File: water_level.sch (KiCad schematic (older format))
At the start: 13 parts, among them U4 TLP293-4

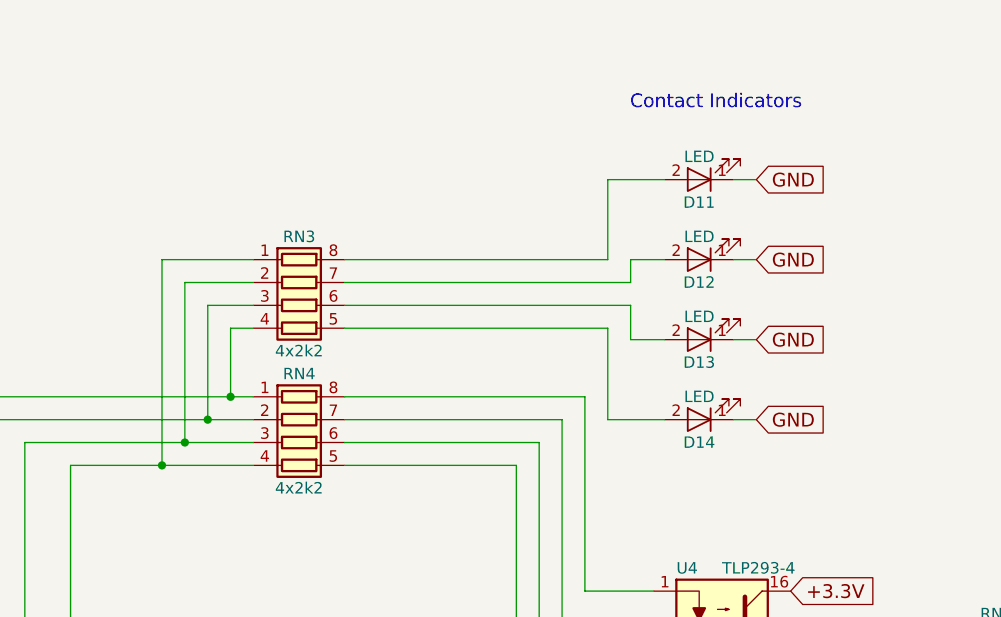
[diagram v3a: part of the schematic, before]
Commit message: the components roughly spaced on the pcb
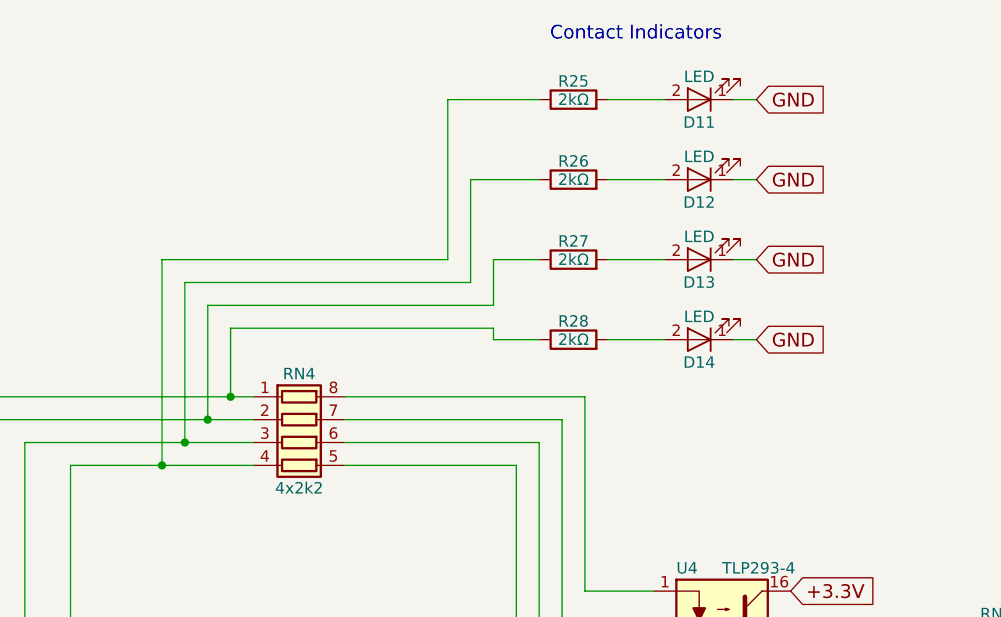
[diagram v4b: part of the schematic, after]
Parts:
- removed RN3: 4x2k2, kilibs:YC164-Yageo-Handsoldering, symbol R_Pack04
- added R25, R26, R27, R28: 2kΩ, Resistors_SMD:R_0603_HandSoldering, symbol R
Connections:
- net at RN4.2 (R2.1), SENS_2.4 (NC): now also R27.1
- net at RN4.1 (R1.1), SENS_1.4 (NC): now also R28.1
- net at RN4.3 (R3.1), SENS_3.4 (NC): now also R26.1
- net at RN4.4 (R4.1), SENS_4.4 (NC): now also R25.1
- net at D13.2 (A): now also R27.2
- net at D14.2 (A): now also R28.2
- net at D12.2 (A): now also R26.2
- net at D11.2 (A): now also R25.2
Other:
- moved on the sheet: D11, D12, D13, D14
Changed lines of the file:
@@
 L LED D13
 U 1 1 59403F87
+P 8000 2100
+F 0 "D13" H 8000 2200 50  0000 C CNN
+F 1 "LED" H 8000 2000 50  0000 C CNN
+F 2 "LEDs:LED_1206" H 8000 2100 50  0001 C CNN
+F 3 "http://hu.farnell.com/lumex/sml-lx15syc-tr/led-yellow-3mm-60mcd-590nm/dp/2062220" H 8000 2100 50  0001 C CNN
+	1    8000 2100
+	-1   0    0    1
+$EndComp
+Wire Wire Line
+	8250 2100 8150 2100
+$Comp
+L LED D14
+U 1 1 5940539F
 P 8000 2450
-F 0 "D13" H 8000 2550 50  0000 C CNN
+F 0 "D14" H 8000 2550 50  0000 C CNN
 F 1 "LED" H 8000 2350 50  0000 C CNN
 F 2 "LEDs:LED_1206" H 8000 2450 50  0001 C CNN
@@
 	8250 2450 8150 2450
 $Comp
-L LED D14
-U 1 1 5940539F
-P 8000 2800
-F 0 "D14" H 8000 2900 50  0000 C CNN
-F 1 "LED" H 8000 2700 50  0000 C CNN
-F 2 "LEDs:LED_1206" H 8000 2800 50  0001 C CNN
-F 3 "http://hu.farnell.com/lumex/sml-lx15syc-tr/led-yellow-3mm-60mcd-590nm/dp/2062220" H 8000 2800 50  0001 C CNN
-	1    8000 2800
-	-1   0    0    1
-$EndComp
-Wire Wire Line
-	8250 2800 8150 2800
-$Comp
 L LED D12
 U 1 1 59405535
-P 8000 2100
-F 0 "D12" H 8000 2200 50  0000 C CNN
-F 1 "LED" H 8000 2000 50  0000 C CNN
-F 2 "LEDs:LED_1206" H 8000 2100 50  0001 C CNN
-F 3 "http://hu.farnell.com/lumex/sml-lx15syc-tr/led-yellow-3mm-60mcd-590nm/dp/2062220" H 8000 2100 50  0001 C CNN
-	1    8000 2100
-	-1   0    0    1
-$EndComp
-Wire Wire Line
-	8250 2100 8150 2100
-$Comp
-L LED D11
-U 1 1 59405613
 P 8000 1750
-F 0 "D11" H 8000 1850 50  0000 C CNN
+F 0 "D12" H 8000 1850 50  0000 C CNN
 F 1 "LED" H 8000 1650 50  0000 C CNN
 F 2 "LEDs:LED_1206" H 8000 1750 50  0001 C CNN
@@
 Wire Wire Line
 	8250 1750 8150 1750
-Text Notes 8450 1450 2    60   ~ 0
+$Comp
+L LED D11
+U 1 1 59405613
+P 8000 1400
+F 0 "D11" H 8000 1500 50  0000 C CNN
+F 1 "LED" H 8000 1300 50  0000 C CNN
+F 2 "LEDs:LED_1206" H 8000 1400 50  0001 C CNN
+F 3 "http://hu.farnell.com/lumex/sml-lx15syc-tr/led-yellow-3mm-60mcd-590nm/dp/2062220" H 8000 1400 50  0001 C CNN
+	1    8000 1400
+	-1   0    0    1
+$EndComp
+Wire Wire Line
+	8250 1400 8150 1400
+Text Notes 8100 1150 2    60   ~ 0
 Contact Indicators
+Text GLabel 8250 1400 2    60   Input ~ 0
+GND
 Text GLabel 8250 1750 2    60   Input ~ 0
 GND
@@
 GND
 Text GLabel 8250 2450 2    60   Input ~ 0
-GND
-Text GLabel 8250 2800 2    60   Input ~ 0
 GND
 Text GLabel 3100 4100 0    60   Input ~ 0
@@
 $EndComp
 Wire Wire Line
-	6450 2100 7600 2100
-Wire Wire Line
-	7600 2100 7600 1750
-Wire Wire Line
-	7600 1750 7850 1750
-Wire Wire Line
-	6450 2200 7700 2200
-Wire Wire Line
-	7700 2200 7700 2100
-Wire Wire Line
-	7700 2100 7850 2100
-Wire Wire Line
-	6450 2300 7700 2300
-Wire Wire Line
-	7700 2300 7700 2450
-Wire Wire Line
-	7700 2450 7850 2450
-Wire Wire Line
-	6450 2400 7600 2400
-Wire Wire Line
-	7600 2400 7600 2800
-Wire Wire Line
-	7600 2800 7850 2800
+	7600 1400 7850 1400
+Wire Wire Line
+	7600 2450 7850 2450
 Wire Wire Line
 	4650 3300 4650 2700
@@
 Connection ~ 5650 3000
 Wire Wire Line
-	5950 2400 6050 2400
-Wire Wire Line
-	5850 2300 6050 2300
-Wire Wire Line
-	5750 2200 6050 2200
-Wire Wire Line
-	5650 2100 6050 2100
-$Comp
-L R_Pack04 RN3
-U 1 1 59A818FC
-P 6250 2300
-F 0 "RN3" V 5950 2300 50  0000 C CNN
-F 1 "4x2k2" V 6450 2300 50  0000 C CNN
-F 2 "kilibs:YC164-Yageo-Handsoldering" V 6525 2300 50  0001 C CNN
-F 3 "http://hu.farnell.com/yageo-phycomp/yc164-jr-072k2l/resistor-array-arv241-1206-2k2/dp/9234535" H 6250 2300 50  0001 C CNN
-	1    6250 2300
-	0    1    1    0
-$EndComp
+	5950 2400 7100 2400
+Wire Wire Line
+	5850 2300 7100 2300
+Wire Wire Line
+	5750 2200 7000 2200
+Wire Wire Line
+	5650 2100 6900 2100
 $Comp
 L R_Pack04 RN4
@@
 Wire Wire Line
 	9050 4050 9050 4650
+$Comp
+L R R25
+U 1 1 59AB9E05
+P 7450 1400
+F 0 "R25" V 7530 1400 50  0000 C CNN
+F 1 "2kΩ" V 7450 1400 50  0000 C CNN
+F 2 "Resistors_SMD:R_0603_HandSoldering" V 7380 1400 50  0001 C CNN
+F 3 "hu.farnell.com/multicomp/mcwr06x2001ftl/res-thick-film-2k-1-0-1w-0603/dp/2447319" H 7450 1400 50  0001 C CNN
+	1    7450 1400
+	0    -1   -1   0
+$EndComp
+$Comp
+L R R26
+U 1 1 59ABA119
+P 7450 1750
+F 0 "R26" V 7530 1750 50  0000 C CNN
+F 1 "2kΩ" V 7450 1750 50  0000 C CNN
+F 2 "Resistors_SMD:R_0603_HandSoldering" V 7380 1750 50  0001 C CNN
+F 3 "hu.farnell.com/multicomp/mcwr06x2001ftl/res-thick-film-2k-1-0-1w-0603/dp/2447319" H 7450 1750 50  0001 C CNN
+	1    7450 1750
+	0    -1   -1   0
+$EndComp
+$Comp
+L R R27
+U 1 1 59ABA15D
+P 7450 2100
+F 0 "R27" V 7530 2100 50  0000 C CNN
+F 1 "2kΩ" V 7450 2100 50  0000 C CNN
+F 2 "Resistors_SMD:R_0603_HandSoldering" V 7380 2100 50  0001 C CNN
+F 3 "hu.farnell.com/multicomp/mcwr06x2001ftl/res-thick-film-2k-1-0-1w-0603/dp/2447319" H 7450 2100 50  0001 C CNN
+	1    7450 2100
+	0    -1   -1   0
+$EndComp
+$Comp
+L R R28
+U 1 1 59ABA30D
+P 7450 2450
+F 0 "R28" V 7530 2450 50  0000 C CNN
+F 1 "2kΩ" V 7450 2450 50  0000 C CNN
+F 2 "Resistors_SMD:R_0603_HandSoldering" V 7380 2450 50  0001 C CNN
+F 3 "hu.farnell.com/multicomp/mcwr06x2001ftl/res-thick-film-2k-1-0-1w-0603/dp/2447319" H 7450 2450 50  0001 C CNN
+	1    7450 2450
+	0    -1   -1   0
+$EndComp
+Wire Wire Line
+	7600 1750 7850 1750
+Wire Wire Line
+	7600 2100 7850 2100
+Wire Wire Line
+	7300 2450 7100 2450
+Wire Wire Line
+	7100 2450 7100 2400
+Wire Wire Line
+	7300 2100 7100 2100
+Wire Wire Line
+	7100 2100 7100 2300
+Wire Wire Line
+	7300 1750 7000 1750
+Wire Wire Line
+	7000 1750 7000 2200
+Wire Wire Line
+	7300 1400 6900 1400
+Wire Wire Line
+	6900 1400 6900 2100
 $EndSCHEMATC

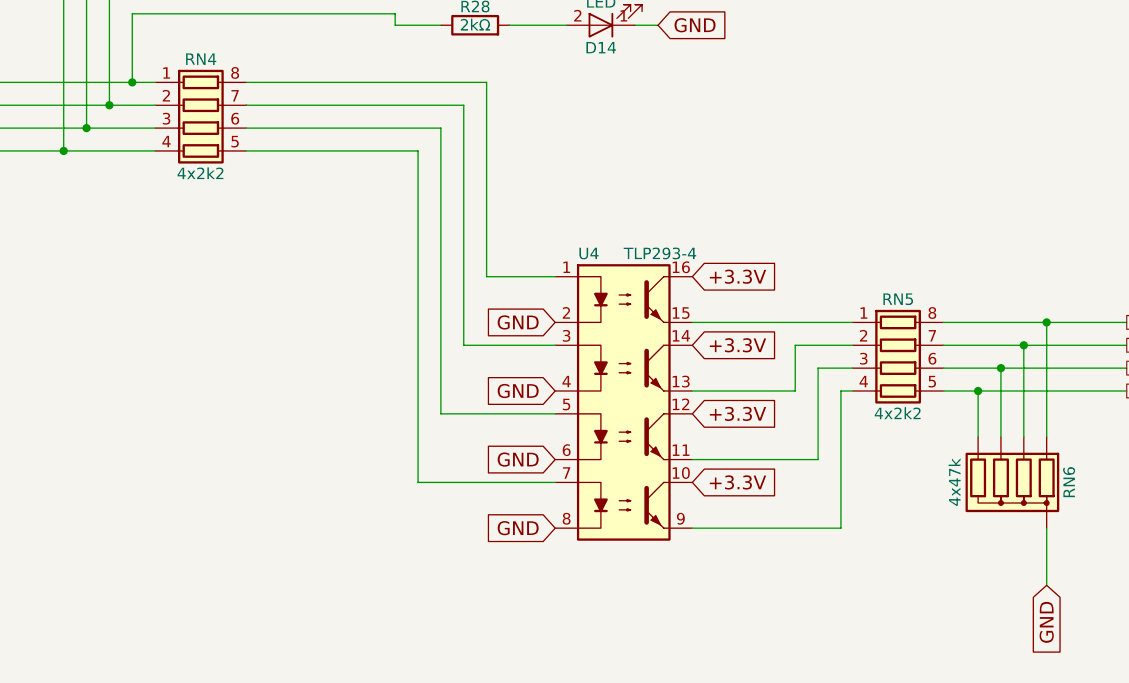
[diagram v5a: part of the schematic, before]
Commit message: This version contains the final revision before the part footprint verification.
- The fuse is now moved outside of the power module before any parts
- The wifi module has an additional pair of 22R differential resistors
- The minor moves in the power power supply of the wifi module
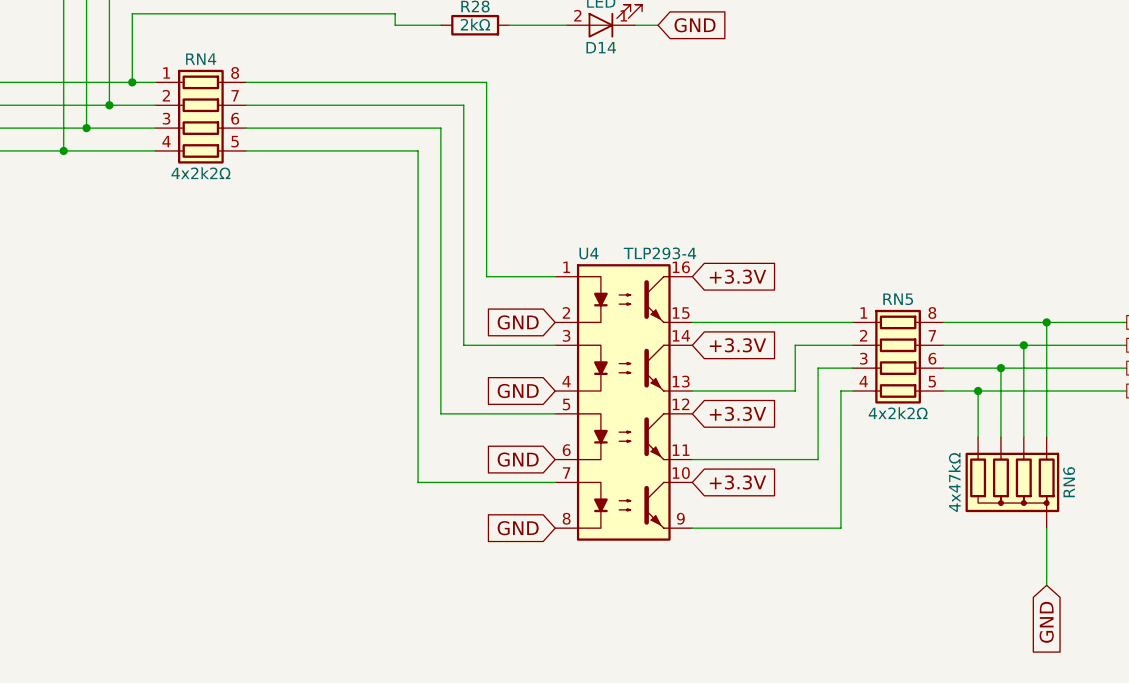
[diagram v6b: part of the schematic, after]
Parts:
- RN4, RN5: value 4x2k2 -> 4x2k2Ω
- RN6: value 4x47k -> 4x47kΩ
- U4: footprint Housings_SOIC:SOIC-16_3.9x9.9mm_Pitch1.27mm -> Housings_DIP:DIP-16_W7.62mm_SMDSocket_SmallPads; alt_soic (none) -> http://hu.farnell.com/toshiba/tlp293-4-gb/optocoupler-photo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
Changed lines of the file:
@@
 P 9750 4450
 F 0 "RN6" V 9450 4450 50  0000 C CNN
-F 1 "4x47k" V 9950 4450 50  0000 C CNN
+F 1 "4x47kΩ" V 9950 4450 50  0000 C CNN
 F 2 "water:YC158-Yageo-Handsoldering" V 10025 4450 50  0001 C CNN
 F 3 "http://hu.farnell.com/yageo-phycomp/yc158tjr-0747kl/resistor-network-rna310-1206-47k/dp/9236279" H 9750 4450 50  0001 C CNN
@@
 F 0 "U4" H 7900 4850 50  0000 L CNN
 F 1 "TLP293-4" H 8100 4850 50  0000 L CNN
-F 2 "Housings_SOIC:SOIC-16_3.9x9.9mm_Pitch1.27mm" H 7900 3550 50  0001 L CIN
-F 3 "http://hu.farnell.com/toshiba/tlp293-4-gb/optocoupler-phototrans-3-75kv/dp/2524320" H 8100 4050 50  0001 L CNN
+F 2 "Housings_DIP:DIP-16_W7.62mm_SMDSocket_SmallPads" H 7900 3550 50  0001 L CIN
+F 3 "http://hu.farnell.com/broadcom-limited/acpl-847-300e/optocoupler-transistor-o-p-5kv/dp/1339044" H 8100 4050 50  0001 L CNN
+F 4 "http://hu.farnell.com/toshiba/tlp293-4-gb/optocoupler-phototrans-3-75kv/dp/2524320" H 8100 4150 60  0001 C CNN "alt_soic"
 	1    8100 4150
 	1    0    0    -1
@@
 P 6250 2900
 F 0 "RN4" V 5950 2900 50  0000 C CNN
-F 1 "4x2k2" V 6450 2900 50  0000 C CNN
+F 1 "4x2k2Ω" V 6450 2900 50  0000 C CNN
 F 2 "kilibs:YC164-Yageo-Handsoldering" V 6525 2900 50  0001 C CNN
 F 3 "http://hu.farnell.com/yageo-phycomp/yc164-jr-072k2l/resistor-array-arv241-1206-2k2/dp/9234535" H 6250 2900 50  0001 C CNN
@@
 P 9300 3950
 F 0 "RN5" V 9000 3950 50  0000 C CNN
-F 1 "4x2k2" V 9500 3950 50  0000 C CNN
+F 1 "4x2k2Ω" V 9500 3950 50  0000 C CNN
 F 2 "kilibs:YC164-Yageo-Handsoldering" V 9575 3950 50  0001 C CNN
 F 3 "http://hu.farnell.com/yageo-phycomp/yc164-jr-072k2l/resistor-array-arv241-1206-2k2/dp/9234535" H 9300 3950 50  0001 C CNN

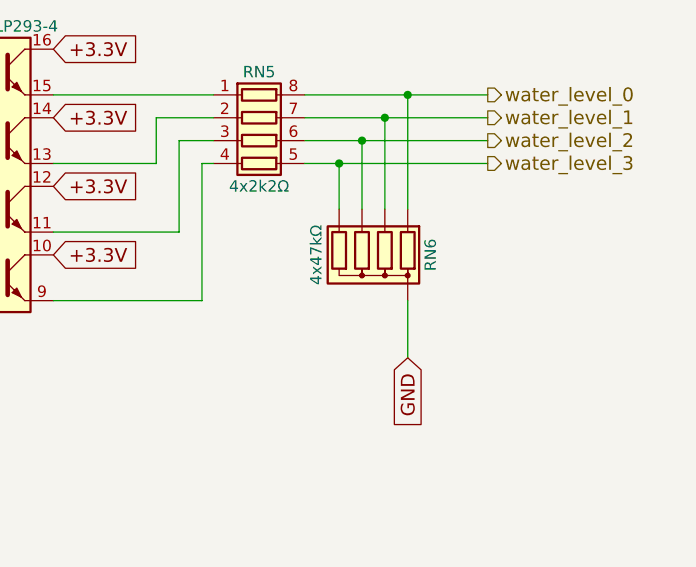
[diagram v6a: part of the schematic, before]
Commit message: I have replaced the 8xresistors to 4resistors because the distance between the pads was not big enough for the 3um copper layers
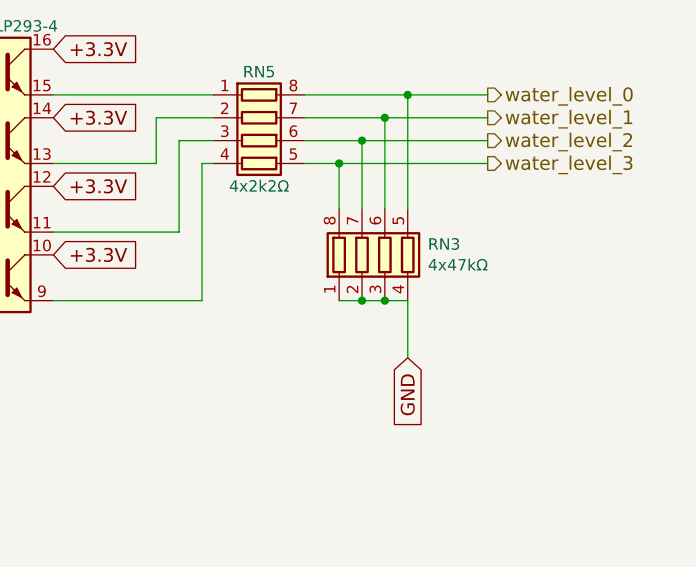
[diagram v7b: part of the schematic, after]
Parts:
- removed RN6: 4x47kΩ, water:YC158-Yageo-Handsoldering, symbol R_Network04
- added RN3: 4x47kΩ, kilibs:YC164-Yageo-Handsoldering, symbol R_Pack04
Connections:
- net GND: now also RN3.1 (R1.1), RN3.2 (R2.1), RN3.3 (R3.1), RN3.4 (R4.1)
- net water_level_0: now also RN3.5 (R4.2)
- net water_level_1: now also RN3.6 (R3.2)
- net water_level_2: now also RN3.7 (R2.2)
- net water_level_3: now also RN3.8 (R1.2)
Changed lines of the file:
@@
 Text GLabel 3100 6950 0    60   Input ~ 0
 +5V
-$Comp
-L R_Network04 RN6
-U 1 1 59A52B59
-P 9750 4450
-F 0 "RN6" V 9450 4450 50  0000 C CNN
-F 1 "4x47kΩ" V 9950 4450 50  0000 C CNN
-F 2 "water:YC158-Yageo-Handsoldering" V 10025 4450 50  0001 C CNN
-F 3 "http://hu.farnell.com/yageo-phycomp/yc158tjr-0747kl/resistor-network-rna310-1206-47k/dp/9236279" H 9750 4450 50  0001 C CNN
-	1    9750 4450
-	-1   0    0    1
-$EndComp
 Wire Wire Line
 	7600 1400 7850 1400
@@
 Text GLabel 9950 4900 3    60   Input ~ 0
 GND
-Wire Wire Line
-	9950 4900 9950 4650
 Wire Wire Line
 	9650 4250 9650 4050
@@
 Wire Wire Line
 	6900 1400 6900 2100
+Connection ~ 9750 4650
+Connection ~ 9850 4650
+$Comp
+L R_Pack04 RN3
+U 1 1 59B14285
+P 9850 4450
+F 0 "RN3" H 10038 4496 50  0000 L CNN
+F 1 "4x47kΩ" H 10038 4405 50  0000 L CNN
+F 2 "kilibs:YC164-Yageo-Handsoldering" V 10125 4450 50  0001 C CNN
+F 3 "http://hu.farnell.com/yageo-phycomp/yc164-jr-0747kl/resistor-array-arv241-1206-47k/dp/9234594" H 9850 4450 50  0001 C CNN
+	1    9850 4450
+	1    0    0    -1
+$EndComp
+Wire Wire Line
+	9950 4650 9950 4900
+Wire Wire Line
+	9650 4650 9950 4650
 $EndSCHEMATC
